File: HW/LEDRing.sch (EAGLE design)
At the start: 48 parts, among them U1 ATMEGA328P-AU, U2 MCP73831, U3 MIC5219 3.3V, U4 MMA8452Q, U5 FT231XS, Y1 16MHZ

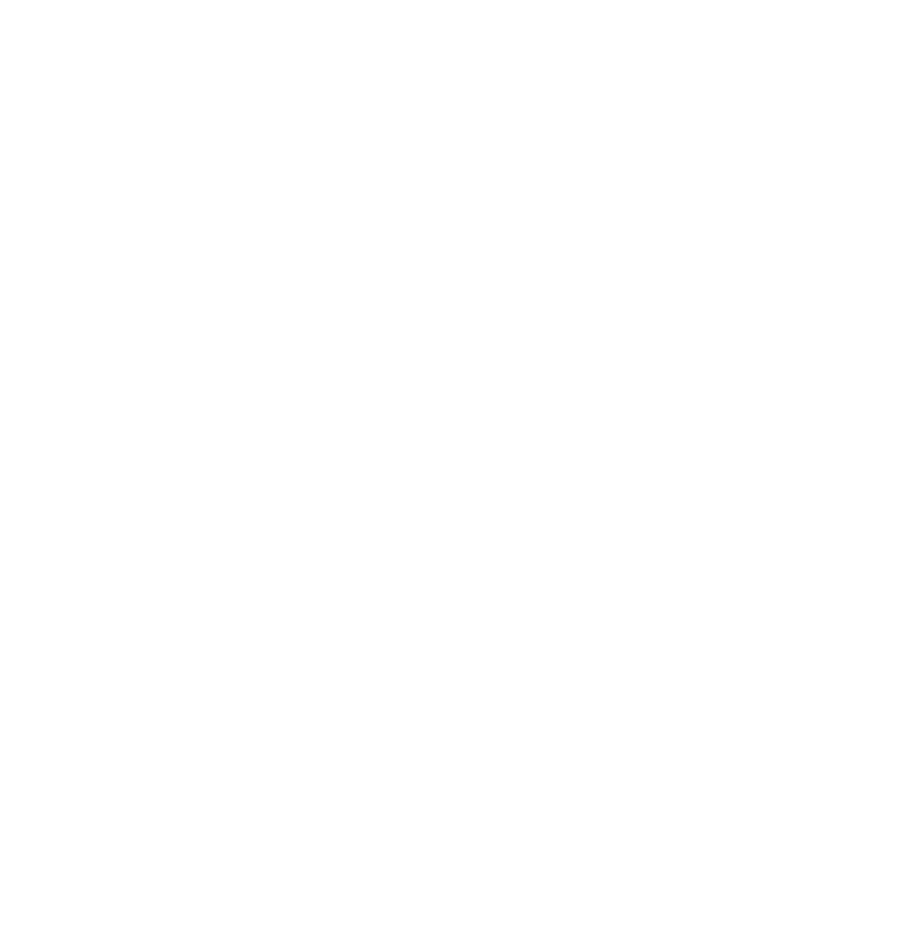
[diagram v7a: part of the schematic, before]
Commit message: Updating all files. I've started adding a motor driver (vibration motor).
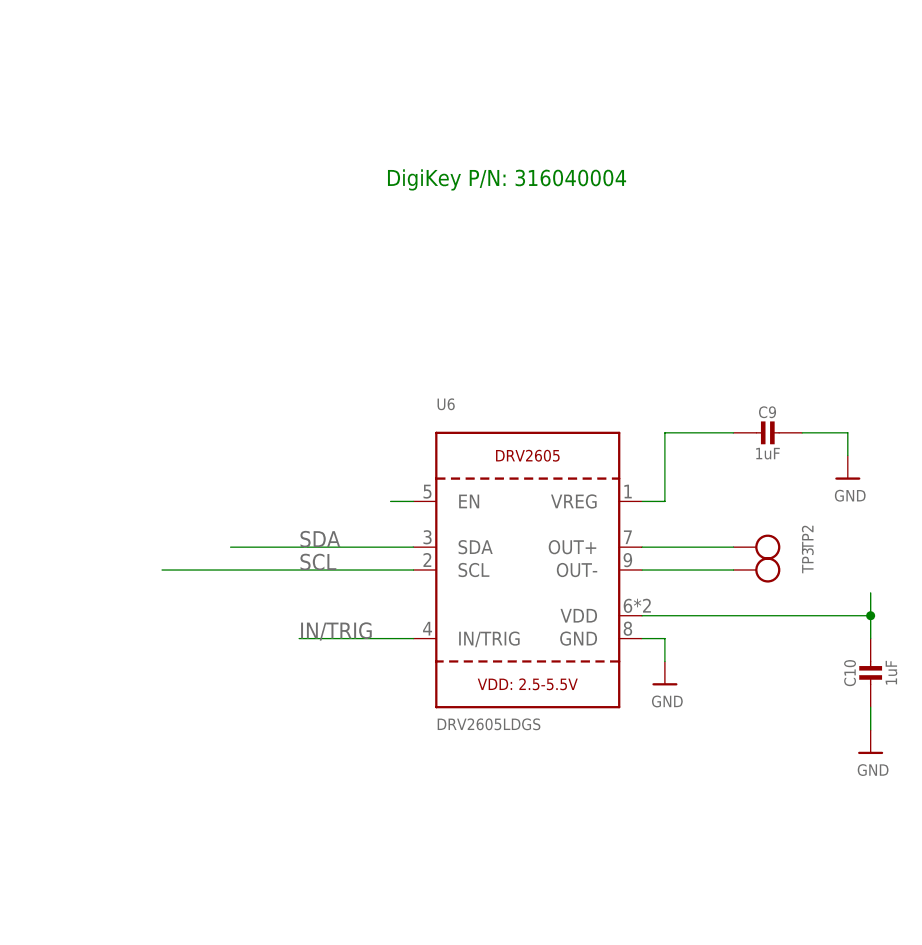
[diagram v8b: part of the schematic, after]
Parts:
- added C10, C9: 1uF, microbuilder:CAP_CERAMIC0805-NOOUTLINE
- added TP2, TP3: (no value), microbuilder:TESTPOINTPAD2MM
- added U6: DRV2605LDGS, microbuilder:DRV2605_SOP
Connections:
- new net IN/TRIG: U6.IN/TRIG
- new net N$32: C9.2, U6.VREG
- new net N$36: C10.1, U6.VDD
- new net N$37: U6.EN
- new net OUT+: TP2.P$1, U6.OUT+
- new net OUT-: TP3.P$1, U6.OUT-
- net GND: now also C10.2, C9.1, U6.GND
- net SCL: now also U6.SCL
- net SDA: now also U6.SDA
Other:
- note added: "DigiKey P/N: 316040004"
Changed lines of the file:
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@@
 <?xml version="1.0" encoding="utf-8"?>
 <!DOCTYPE eagle SYSTEM "eagle.dtd">
-<eagle version="7.3.0">
+<eagle version="8.0.0">
 <drawing>
 <settings>
@@
 <part name="R13" library="SparkFun-Passives" deviceset="RESISTOR" device="0603-RES" value="10k"/>
 <part name="TP1" library="SparkFun-Passives" deviceset="TEST-POINT" device="3"/>
+<part name="U6" library="microbuilder" deviceset="DRV2605" device="_SOP" value="DRV2605LDGS"/>
+<part name="U$10" library="microbuilder" deviceset="GND" device=""/>
+<part name="C9" library="microbuilder" deviceset="CAP_CERAMIC" device="0805-NOOUTLINE" value="1uF"/>
+<part name="U$8" library="microbuilder" deviceset="GND" device=""/>
+<part name="C10" library="microbuilder" deviceset="CAP_CERAMIC" device="0805-NOOUTLINE" value="1uF"/>
+<part name="U$12" library="microbuilder" deviceset="GND" device=""/>
+<part name="TP2" library="microbuilder" deviceset="TESTPOINT" device="PAD2MM"/>
+<part name="TP3" library="microbuilder" deviceset="TESTPOINT" device="PAD2MM"/>
 </parts>
 <sheets>
@@
 <plain>
 <text x="25.4" y="111.76" size="1.778" layer="97">Battery: 1.185 x 1.42</text>
+<text x="320.04" y="60.96" size="1.778" layer="91">DigiKey P/N: 316040004</text>
 </plain>
 <instances>
@@
 <instance part="R13" gate="G$1" x="154.94" y="20.32" rot="R90"/>
 <instance part="TP1" gate="G$1" x="-76.2" y="99.06" rot="R270"/>
+<instance part="U6" gate="G$1" x="335.788" y="18.288"/>
+<instance part="U$10" gate="G$1" x="351.028" y="5.588"/>
+<instance part="C9" gate="G$1" x="361.188" y="33.528" rot="R270"/>
+<instance part="U$8" gate="G$1" x="371.348" y="28.448"/>
+<instance part="C10" gate="G$1" x="373.888" y="5.588"/>
+<instance part="U$12" gate="G$1" x="373.888" y="-2.032"/>
+<instance part="TP2" gate="G$1" x="358.648" y="20.828" rot="R270"/>
+<instance part="TP3" gate="G$1" x="358.648" y="18.288" rot="R270"/>
 </instances>
 <busses>
@@
 <junction x="-27.94" y="78.74"/>
 <pinref part="GND20" gate="1" pin="GND"/>
+</segment>
+<segment>
+<pinref part="U6" gate="G$1" pin="GND"/>
+<pinref part="U$10" gate="G$1" pin="GND"/>
+<wire x1="348.488" y1="10.668" x2="351.028" y2="10.668" width="0.1524" layer="91"/>
+<wire x1="351.028" y1="10.668" x2="351.028" y2="8.128" width="0.1524" layer="91"/>
+</segment>
+<segment>
+<pinref part="C9" gate="G$1" pin="1"/>
+<pinref part="U$8" gate="G$1" pin="GND"/>
+<wire x1="366.268" y1="33.528" x2="371.348" y2="33.528" width="0.1524" layer="91"/>
+<wire x1="371.348" y1="33.528" x2="371.348" y2="30.988" width="0.1524" layer="91"/>
+</segment>
+<segment>
+<pinref part="C10" gate="G$1" pin="2"/>
+<pinref part="U$12" gate="G$1" pin="GND"/>
+<wire x1="373.888" y1="3.048" x2="373.888" y2="0.508" width="0.1524" layer="91"/>
 </segment>
 </net>
@@
 <label x="106.68" y="20.32" size="1.778" layer="95"/>
 </segment>
+<segment>
+<pinref part="U6" gate="G$1" pin="SCL"/>
+<wire x1="323.088" y1="18.288" x2="295.148" y2="18.288" width="0.1524" layer="91"/>
+<label x="310.388" y="18.288" size="1.778" layer="95"/>
+</segment>
 </net>
 <net name="SDA" class="0">
@@
 <wire x1="104.14" y1="17.78" x2="106.68" y2="17.78" width="0.1524" layer="91"/>
 <label x="106.68" y="17.78" size="1.778" layer="95"/>
+</segment>
+<segment>
+<pinref part="U6" gate="G$1" pin="SDA"/>
+<wire x1="323.088" y1="20.828" x2="302.768" y2="20.828" width="0.1524" layer="91"/>
+<label x="310.388" y="20.828" size="1.778" layer="95"/>
 </segment>
 </net>
@@
 </segment>
 </net>
+<net name="OUT+" class="0">
+<segment>
+<pinref part="U6" gate="G$1" pin="OUT+"/>
+<wire x1="348.488" y1="20.828" x2="358.648" y2="20.828" width="0.1524" layer="91"/>
+<pinref part="TP2" gate="G$1" pin="P$1"/>
+</segment>
+</net>
+<net name="OUT-" class="0">
+<segment>
+<pinref part="U6" gate="G$1" pin="OUT-"/>
+<wire x1="348.488" y1="18.288" x2="358.648" y2="18.288" width="0.1524" layer="91"/>
+<pinref part="TP3" gate="G$1" pin="P$1"/>
+</segment>
+</net>
+<net name="N$32" class="0">
+<segment>
+<pinref part="U6" gate="G$1" pin="VREG"/>
+<wire x1="348.488" y1="25.908" x2="351.028" y2="25.908" width="0.1524" layer="91"/>
+<wire x1="351.028" y1="25.908" x2="351.028" y2="33.528" width="0.1524" layer="91"/>
+<pinref part="C9" gate="G$1" pin="2"/>
+<wire x1="351.028" y1="33.528" x2="358.648" y2="33.528" width="0.1524" layer="91"/>
+</segment>
+</net>
+<net name="IN/TRIG" class="0">
+<segment>
+<pinref part="U6" gate="G$1" pin="IN/TRIG"/>
+<wire x1="323.088" y1="10.668" x2="310.388" y2="10.668" width="0.1524" layer="91"/>
+<label x="310.388" y="10.668" size="1.778" layer="95"/>
+</segment>
+</net>
+<net name="N$36" class="0">
+<segment>
+<pinref part="U6" gate="G$1" pin="VDD"/>
+<wire x1="348.488" y1="13.208" x2="373.888" y2="13.208" width="0.1524" layer="91"/>
+<wire x1="373.888" y1="13.208" x2="373.888" y2="15.748" width="0.1524" layer="91"/>
+<pinref part="C10" gate="G$1" pin="1"/>
+<wire x1="373.888" y1="13.208" x2="373.888" y2="10.668" width="0.1524" layer="91"/>
+<junction x="373.888" y="13.208"/>
+</segment>
+</net>
+<net name="N$37" class="0">
+<segment>
+<pinref part="U6" gate="G$1" pin="EN"/>
+<wire x1="323.088" y1="25.908" x2="320.548" y2="25.908" width="0.1524" layer="91"/>
+</segment>
+</net>
